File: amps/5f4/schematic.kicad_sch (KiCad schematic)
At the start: 66 parts, among them T3 45216

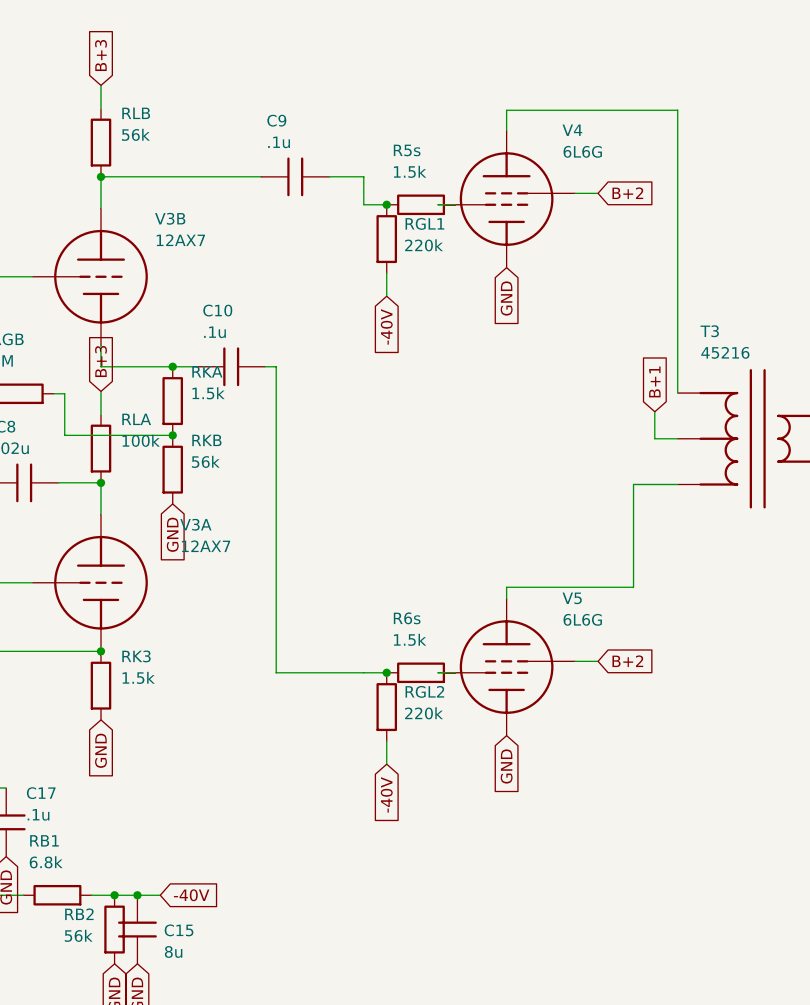
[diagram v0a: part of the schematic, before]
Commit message: Fix: schematic wiring on 5c1, 5e1, 5e4a, 5e5a, 5e6a, 5f4; all six claim equivalence
- 5c1, 5e1: the B+1/B+2/B+3 labels sat 3.56 mm above the filter chain with
  no lead, naming rails the drawing never reached
- 5e4a, 5e5a, 5e6a, 5f4: the 220k grid leak tapped the coupling-cap node;
  the netlist and the factory-derived layouts both return it at the grid
  pin after the 1.5k stopper (coupler -> stopper -> grid, as jtm45 draws
  it); each stopper now lands on the pentode's own grid pin and the leak
  hangs off that junction
- sch_map.yaml schematic_claim: verified on all six -> 37 of 38 sheets are
  hard-gated; 6g5 stays unclaimed (presence-branch DC path is a source
  question, not a declaration)

Co-Authored-By: Claude Fable 5.1 <noreply@anthropic.com>
Claude-Session: https://claude.ai/code/session_01KBMfdh37HmCL2iWcBiL5J1
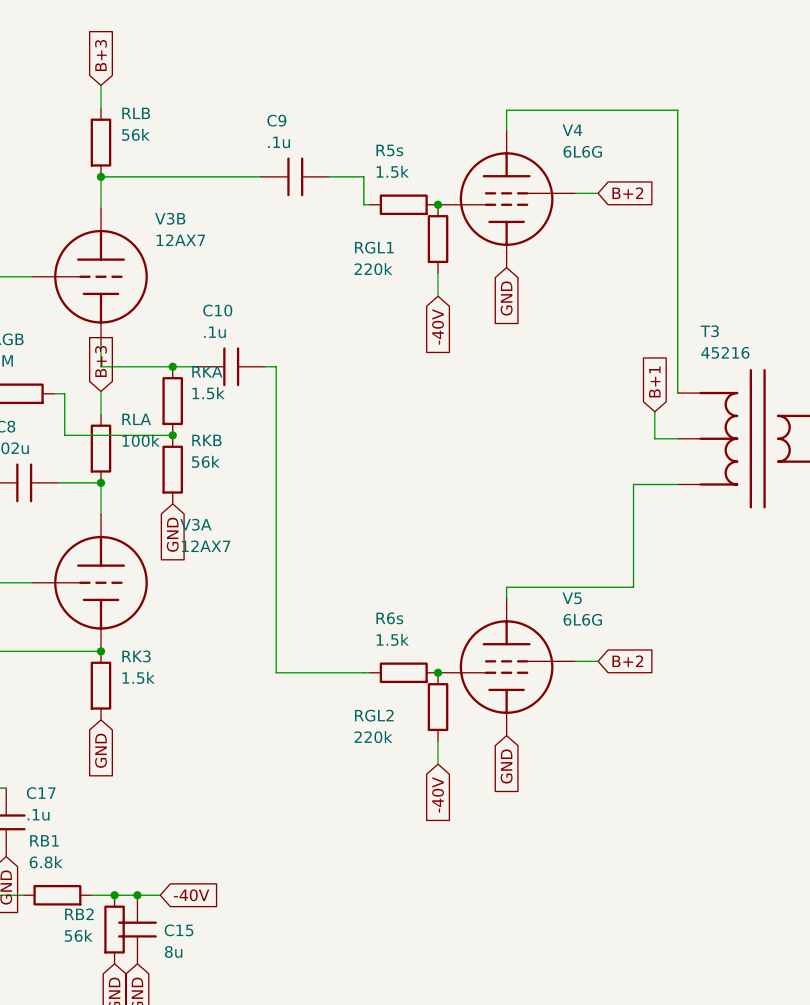
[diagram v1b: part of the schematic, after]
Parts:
- removed RB1: 6.8k, symbol cx:R
- removed RD1, RD2: 10k, symbol cx:R
- added C12, C13: 16u, symbol cx:C
- added D1: SEL, symbol cx:DIODE_SS
- RB1: renamed from D1; value SEL -> 6.8k; symbol cx:DIODE_SS -> cx:R
- RD1: renamed from C12; value 16u -> 10k; symbol cx:C -> cx:R
- RD2: renamed from C13; value 16u -> 10k; symbol cx:C -> cx:R
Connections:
- net -40V: now also RB1.2
- net B+2: now also C12.1
- net B+3: now also RD1.2, C13.1
- net B+4: now also RD2.2
- net GND: now also C12.2, C13.2; no longer RD1.2, RD2.2
- net HT_B: now also D1.1 (A); no longer RB1.1 (A)
- net at C9.2, R5s.1: no longer RGL1.1
- net at R6s.2, V5.2 (G1): now also RGL2.1
- net at R5s.2, V4.2 (G1): now also RGL1.1
- net at C10.2, R6s.1: no longer RGL2.1
- new net: D1.2 (K), RB1.1
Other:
- moved on the sheet: R5s
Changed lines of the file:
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@@
   (wire (pts (xy 196.758 27.178) (xy 196.758 30.278))
     (stroke (width 0) (type default)))
-  (wire (pts (xy 196.758 30.278) (xy 199.298 30.278))
-    (stroke (width 0) (type default)))
-  (symbol (lib_id "cx:R") (at 203.108 30.278 90) (unit 1)
-    (in_bom yes) (on_board yes)
-    (property "Reference" "R5s" (at 199.908 24.278 270) (effects (font (size 1.27 1.27)) (justify left)))
-    (property "Value" "1.5k" (at 199.908 26.678 270) (effects (font (size 1.27 1.27)) (justify left))))
   (symbol (lib_id "cx:PENTODE") (at 212.618 29.643 0) (unit 1)
     (in_bom yes) (on_board yes)
     (property "Reference" "V4" (at 218.818 22.043 0) (effects (font (size 1.27 1.27)) (justify left)))
     (property "Value" "6L6G" (at 218.818 24.443 0) (effects (font (size 1.27 1.27)) (justify left))))
-  (wire (pts (xy 206.918 30.278) (xy 204.998 30.278))
+  (symbol (lib_id "cx:R") (at 201.188 30.278 90) (unit 1)
+    (in_bom yes) (on_board yes)
+    (property "Reference" "R5s" (at 197.988 24.278 270) (effects (font (size 1.27 1.27)) (justify left)))
+    (property "Value" "1.5k" (at 197.988 26.678 270) (effects (font (size 1.27 1.27)) (justify left))))
+  (wire (pts (xy 196.758 30.278) (xy 197.378 30.278))
     (stroke (width 0) (type default)))
-  (junction (at 199.298 30.278) (diameter 0) (color 0 0 0 0))
-  (symbol (lib_id "cx:R") (at 199.298 34.088 0) (unit 1)
+  (junction (at 204.998 30.278) (diameter 0) (color 0 0 0 0))
+  (symbol (lib_id "cx:R") (at 204.998 34.088 0) (unit 1)
     (in_bom yes) (on_board yes)
-    (property "Reference" "RGL1" (at 201.214 32.448 0) (effects (font (size 1.27 1.27)) (justify left)))
-    (property "Value" "220k" (at 201.214 34.848 0) (effects (font (size 1.27 1.27)) (justify left))))
-  (wire (pts (xy 199.298 37.898) (xy 199.298 40.438))
+    (property "Reference" "RGL1" (at 195.598 35.088 0) (effects (font (size 1.27 1.27)) (justify left)))
+    (property "Value" "220k" (at 195.598 37.488 0) (effects (font (size 1.27 1.27)) (justify left))))
+  (wire (pts (xy 204.998 37.898) (xy 204.998 40.438))
     (stroke (width 0) (type default)))
-  (global_label "-40V" (shape input) (at 199.298 40.438 270)
+  (global_label "-40V" (shape input) (at 204.998 40.438 270)
     (effects (font (size 1.27 1.27)) (justify right)))
   (wire (pts (xy 220.238 29.008) (xy 222.778 29.008))
@@
   (wire (pts (xy 187.018 82.278) (xy 196.758 82.278))
     (stroke (width 0) (type default)))
-  (wire (pts (xy 196.758 82.278) (xy 199.298 82.278))
-    (stroke (width 0) (type default)))
-  (symbol (lib_id "cx:R") (at 203.108 82.278 90) (unit 1)
-    (in_bom yes) (on_board yes)
-    (property "Reference" "R6s" (at 199.908 76.278 270) (effects (font (size 1.27 1.27)) (justify left)))
-    (property "Value" "1.5k" (at 199.908 78.678 270) (effects (font (size 1.27 1.27)) (justify left))))
   (symbol (lib_id "cx:PENTODE") (at 212.618 81.643 0) (unit 1)
     (in_bom yes) (on_board yes)
     (property "Reference" "V5" (at 218.818 74.043 0) (effects (font (size 1.27 1.27)) (justify left)))
     (property "Value" "6L6G" (at 218.818 76.443 0) (effects (font (size 1.27 1.27)) (justify left))))
-  (wire (pts (xy 206.918 82.278) (xy 204.998 82.278))
+  (symbol (lib_id "cx:R") (at 201.188 82.278 90) (unit 1)
+    (in_bom yes) (on_board yes)
+    (property "Reference" "R6s" (at 197.988 76.278 270) (effects (font (size 1.27 1.27)) (justify left)))
+    (property "Value" "1.5k" (at 197.988 78.678 270) (effects (font (size 1.27 1.27)) (justify left))))
+  (wire (pts (xy 196.758 82.278) (xy 197.378 82.278))
     (stroke (width 0) (type default)))
-  (junction (at 199.298 82.278) (diameter 0) (color 0 0 0 0))
-  (symbol (lib_id "cx:R") (at 199.298 86.088 0) (unit 1)
+  (junction (at 204.998 82.278) (diameter 0) (color 0 0 0 0))
+  (symbol (lib_id "cx:R") (at 204.998 86.088 0) (unit 1)
     (in_bom yes) (on_board yes)
-    (property "Reference" "RGL2" (at 201.214 84.448 0) (effects (font (size 1.27 1.27)) (justify left)))
-    (property "Value" "220k" (at 201.214 86.848 0) (effects (font (size 1.27 1.27)) (justify left))))
-  (wire (pts (xy 199.298 89.898) (xy 199.298 92.438))
+    (property "Reference" "RGL2" (at 195.598 87.088 0) (effects (font (size 1.27 1.27)) (justify left)))
+    (property "Value" "220k" (at 195.598 89.488 0) (effects (font (size 1.27 1.27)) (justify left))))
+  (wire (pts (xy 204.998 89.898) (xy 204.998 92.438))
     (stroke (width 0) (type default)))
-  (global_label "-40V" (shape input) (at 199.298 92.438 270)
+  (global_label "-40V" (shape input) (at 204.998 92.438 270)
     (effects (font (size 1.27 1.27)) (justify right)))
   (wire (pts (xy 220.238 81.008) (xy 222.778 81.008))

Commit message: Add: real tube pin numbers and readable valve glyphs on every schematic
Phase B of the drawing program. A factory service sheet numbers every tube
pin, because the number is what a technician puts a probe on. This corpus
printed none, and the numbers hidden in its symbols were positional
placeholders (P=1, G=2, K=3) that would have published a 6V6GT's plate as
pin 1 when it is pin 3.

1055 electrodes now carry the real number, 1027 lettered (27 are shared
filaments deduped, 1 dropped for want of clear space on the 6G2). Resolved per
instance from reference/tubes/<slug>.yaml through the same alias resolution the
layout renderer uses, so a 12AX7 section and a 6SL7 section each get their own
basing. A valve whose basing the corpus does not carry prints nothing rather
than a wrong number.

Section letters and basing units are now separate things, which cost a detour
worth recording. The RCA 12AX7-A sheet reads "Pin 1 - Plate of Unit No.2 ...
Pin 6 - Plate of Unit No.1", so unit numbering is not pin order; the 5Y3 and
GZ34 number their units in opposite pin order, so nothing positional can
express it. But the section LETTER is a designator, not a basing fact: this
corpus, like every technician, calls the first stage in signal order V1A, and
five amps' prose already did. On four amps the factory sheets put that first
stage on the other half -- the AA764's own schematic prints +200 V on pin 1 --
so those drawings now state their unit explicitly, each citing its source, and
no letter, netlist, parts list or layout comment changed. 183 layout comments
agree with the printed numbers, 0 disagree. A guard fires if two halves of one
bottle resolve to the same unit, which is exactly how this was found.

Glyphs: the cathode gains a bracket and filament hairpin so it can no longer be
confused with the plate bar, the pentode's screen sits on its own row, and a
rectifier draws as one envelope over its sections instead of two apparent
bottles. Line weights are scaled per sheet to a co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
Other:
- note added: "1"
- note added: "2"
- note added: "2,8"
- note added: "3"
- note added: "4"
- note added: "5"
- note added: "6"
- note added: "7"
- note added: "8"

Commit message: Fix: schematic sheet notes no longer name repository files
Thirty-seven committed sheets rendered footnotes and section notes such as
"Heaters and PT primary omitted — see netlist.cir and meta.yaml" or
"excluded from netlist.cir (notes.md)" to visitors through KiCanvas. The
prose sweeps never counted sheets. Rewritten in the site's own words — the
netlist, the sources list, the circuit story, the parts list, the board
drawing — in 59 strings across 33 draw scripts, keeping every technical
claim as it was; the three tone sheets (6G4, 6G5, 6G6-B) are under repair
elsewhere and keep theirs for now. The sweep touched only strings passed to
the sheet's note, text, caption and footnote calls, never a path or a value.

Gates: check_schematics 40/0, connectivity 0 isolated pins;
verify_schematic_nets 40 clean; only the regenerated sheets and their served
copies changed.

Co-Authored-By: Claude Fable 5.1 <noreply@anthropic.com>
Claude-Session: https://claude.ai/code/session_01KBMfdh37HmCL2iWcBiL5J1
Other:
- note added: "Heaters, PT primary and standby omitted — see the netlist and the sources list"
- note removed: "Heaters, PT primary and standby omitted — see netlist.cir and meta.yaml"
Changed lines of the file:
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@@
   (text "4" (at 46.478 107.708 0)
     (effects (font (size 1.1 1.1)) (justify left)))
-  (text "Heaters, PT primary and standby omitted — see netlist.cir and meta.yaml" (at 12.7 142.856 0)
+  (text "Heaters, PT primary and standby omitted — see the netlist and the sources list" (at 12.7 142.856 0)
     (effects (font (size 1.2 1.2)) (justify left)))
   (sheet_instances (path "/" (page "1")))

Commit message: Fix: state the datasheet unit on 17 dual-triode sections whose sheets printed the other half's pin numbers
The sheet-vs-board gate reported these sockets as SECTION-SWAP; the
2026-09-10 source-read triage found the BOARD right on every one of them
(and both surfaces wrong on the 5G9 tremolo bottle). Each sheet had
lettered the section on the default map (A -> unit 1 -> pins 6/7/8) where
the factory drawing puts that stage on 1/2/3. The draw scripts now state
`unit=` on both halves, with the source cited beside the call, so the
printed socket numbers are the factory's:

- 5f4 V3: driver V3A -> 1/2/3, cathodyne V3B -> 6/7/8
  (crop 5f4-V3-layout-trace.png: +213 V driver plate -> pin 1, +270 V -> 6)
- 5f8a V3: 82k half V3A -> 1/2/3, 100k half V3B -> 6/7/8
  (crop 5f8a-V3-layout-trace.png: +225 -> 6, +19 -> 2, +28.5 -> 8)
- 6161 V1: channel 1 V1A -> 1/2/3 (crop 6161-V1-ch1.png prints 1/2/3);
  6161 V2: 1 MEG-grid half V2A -> 1/2/3, paraphase V2B -> 6/7/8
  (crop 6161-V2.png / 6161-V2-right.png)
- 6g3 V3: 82k half V3A -> 1/2/3 (crop 6g3-V3-layout-wires.png: +230 -> 1,
  +225 -> 6, +20 -> 7)
- aa1164 V3: recovery V3A -> 1/2/3, mixer V3B -> 6/7/8
  (crops aa1164-V3A-recovery-schem.png, aa1164-V3B-mixer-schem.png)
- aa864-bassman V1/V2: input stages 2/1/3, second stages 7/6/8; V4: the
  .1/500 pF-fed 82k half 2/1/3 (crops aa864-V1A-input.png,
  aa864-V1B-second.png, aa864-V2A-input.png, aa864-V2B-second.png,
  aa864-V4-PI.png)
- ab165 V1/V2/V4: same pattern (crops ab165-V1A-input.png,
  ab165-V1B-second.png, ab165-V2A-input.png, ab165-V2B-second.png,
  ab165-V4-PI.png)
- ab763-super V1/V2: slope-plate +270 V -> pin 1 (input stage), .047
  plate -> 6 (crops ab763-super-V1-layout-sh.png, ab763-super-V2-layout-sh.png)
- dr103 V2/V3: gain stages 6/7/8, cathode followers 1/2/3 (crops
  dr103-V2-huss.png, dr103-V3-huss.png — the Huss redraw, not a factory
  print; noted in the script)
- 5g9 V3: oscillator V3A -> 1/2/3, follower V3B -> 6/7/8 (crops
  5g9-V3-strap71-zoom.png, 5g9-V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
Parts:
- V3A: Basing_unit (none) -> 2
- V3B: Basing_unit (none) -> 1
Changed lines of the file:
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@@
     (in_bom yes) (on_board yes)
     (property "Reference" "V3A" (at 176.348 65.878 0) (effects (font (size 1.27 1.27)) (justify left)))
-    (property "Value" "12AX7" (at 176.348 68.278 0) (effects (font (size 1.27 1.27)) (justify left))))
+    (property "Value" "12AX7" (at 176.348 68.278 0) (effects (font (size 1.27 1.27)) (justify left)))
+    (property "Basing_unit" "2" (at 176.348 70.678 0) (effects (font (size 1.27 1.27)) hide)))
   (wire (pts (xy 154.018 72.278) (xy 159.928 72.278))
     (stroke (width 0) (type default)))
@@
     (in_bom yes) (on_board yes)
     (property "Reference" "V3B" (at 173.548 31.878 0) (effects (font (size 1.27 1.27)) (justify left)))
-    (property "Value" "12AX7" (at 173.548 34.278 0) (effects (font (size 1.27 1.27)) (justify left))))
+    (property "Value" "12AX7" (at 173.548 34.278 0) (effects (font (size 1.27 1.27)) (justify left)))
+    (property "Basing_unit" "1" (at 173.548 36.678 0) (effects (font (size 1.27 1.27)) hide)))
   (wire (pts (xy 167.548 64.658) (xy 167.548 61.178))
     (stroke (width 0) (type default)))
@@
   (text "3" (at 108.708 61.628 0)
     (effects (font (size 1.1 1.1)) (justify left)))
-  (text "6" (at 168.398 65.928 0)
-    (effects (font (size 1.1 1.1)) (justify left)))
-  (text "7" (at 160.601 70.878 0)
-    (effects (font (size 1.1 1.1)) (justify left)))
-  (text "8" (at 168.398 78.628 0)
-    (effects (font (size 1.1 1.1)) (justify left)))
-  (text "1" (at 168.398 31.928 0)
-    (effects (font (size 1.1 1.1)) (justify left)))
-  (text "2" (at 160.601 36.878 0)
-    (effects (font (size 1.1 1.1)) (justify left)))
-  (text "3" (at 169.848 44.628 0)
+  (text "1" (at 168.398 65.928 0)
+    (effects (font (size 1.1 1.1)) (justify left)))
+  (text "2" (at 160.601 70.878 0)
+    (effects (font (size 1.1 1.1)) (justify left)))
+  (text "3" (at 168.398 78.628 0)
+    (effects (font (size 1.1 1.1)) (justify left)))
+  (text "6" (at 168.398 31.928 0)
+    (effects (font (size 1.1 1.1)) (justify left)))
+  (text "7" (at 160.601 36.878 0)
+    (effects (font (size 1.1 1.1)) (justify left)))
+  (text "8" (at 169.848 44.628 0)
     (effects (font (size 1.1 1.1)) (justify left)))
   (text "3" (at 213.468 23.293 0)

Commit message: Fix: draw the 1 MΩ input grid leak on the jack-1 tip node, not the grid, on eight tweed/Champ sheets
Every tweed and Champ factory sheet hangs the 1 MΩ from the jack-1 tip
node (the node the jack-2 shorting contact also lands on) to ground, and
runs the 68 K stoppers from the jack tips to the grid. These eight sheets
drew the 1 MΩ on the GRID side of the stopper — one copy-pasted idiom in
four scripts and its cousins in four more; there is no shared helper, so
each script is fixed where it draws the block. The stopper is declared
DC-transparent (layout net_map.series_bridge), so the netlist sees one node
either way and verify_schematic_nets stays 40 clean; the sheet-vs-board
gate, which compares the drawings to each other, drops all twelve
MISPLACED findings (RG1/RG2 on 5e4a, 5e5a, 5f4, 5f6; R3 on 5f2a, aa764,
aa764-vibro; R1 on 5f1). 5f10's jack chain is a separate task.

Crops read: 5e4a-RG1-RG2-input.png, 5e5a-RG1-RG2-input.png,
5f4-RG1-input.png, 5f6-RG1-RG2-input.png, 5f2a-R3-input.png,
5f1-R1-input.png, aa764-R3-input.png, aa764-vibro-R3-input.png — each
prints "1 MEG." from the jack-1 tip to ground with the 68K pair to the grid.

Geometry: the four two-channel sheets hang the leak from the stopper's
jack-side pin; 5f1 drops it from the INPUT line; 5f2a and the two Champs
stand it upward off the jack-1 line because the jack-2 line runs 8–12 mm
below. Previews read cleanly. The circuit stories already say the leaks
mount at the jacks, so no prose changed.

Gates: check_schematics 40/0 (0 isolated), verify_schematic_nets 40
clean, validate/value-consistency/era-values clean, regenerate-all leaves
every other sheet byte-identical. verify_sheet_vs_board misplaced 98 -> 86.

Co-Authored-By: Claude Fable 5.1 <noreply@anthropic.com>
Claude-Session: https://claude.ai/code/session_01KBMfdh37HmCL2iWcBiL5J1
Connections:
- net CH1: now also RG1.1
- net CH2: now also RG2.1
- net at R1s.2, V1A.2 (G): no longer RG1.1
- net at R2s.2, V1B.2 (G): no longer RG2.1
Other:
- moved on the sheet: RG1, RG2
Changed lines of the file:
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@@
   (wire (pts (xy 29.118 38.278) (xy 32.928 38.278))
     (stroke (width 0) (type default)))
-  (junction (at 29.118 38.278) (diameter 1.013) (color 0 0 0 0))
-  (symbol (lib_id "cx:R") (at 29.118 42.088 0) (unit 1)
+  (junction (at 21.498 38.278) (diameter 1.013) (color 0 0 0 0))
+  (symbol (lib_id "cx:R") (at 21.498 42.088 0) (unit 1)
     (in_bom yes) (on_board yes)
-    (property "Reference" "RG1" (at 31.318 38.888 0) (effects (font (size 1.27 1.27)) (justify left)))
-    (property "Value" "1M" (at 31.318 41.288 0) (effects (font (size 1.27 1.27)) (justify left))))
-  (global_label "GND" (shape input) (at 29.118 45.898 270)
+    (property "Reference" "RG1" (at 23.698 42.088 0) (effects (font (size 1.27 1.27)) (justify left)))
+    (property "Value" "1M" (at 23.698 44.488 0) (effects (font (size 1.27 1.27)) (justify left))))
+  (global_label "GND" (shape input) (at 21.498 45.898 270)
     (effects (font (size 1.27 1.27)) (justify right)))
   (wire (pts (xy 40.548 30.658) (xy 40.548 27.178))
@@
   (wire (pts (xy 29.118 72.278) (xy 32.928 72.278))
     (stroke (width 0) (type default)))
-  (junction (at 29.118 72.278) (diameter 1.013) (color 0 0 0 0))
-  (symbol (lib_id "cx:R") (at 29.118 76.088 0) (unit 1)
+  (junction (at 21.498 72.278) (diameter 1.013) (color 0 0 0 0))
+  (symbol (lib_id "cx:R") (at 21.498 76.088 0) (unit 1)
     (in_bom yes) (on_board yes)
-    (property "Reference" "RG2" (at 31.318 72.888 0) (effects (font (size 1.27 1.27)) (justify left)))
-    (property "Value" "1M" (at 31.318 75.288 0) (effects (font (size 1.27 1.27)) (justify left))))
-  (global_label "GND" (shape input) (at 29.118 79.898 270)
+    (property "Reference" "RG2" (at 23.698 76.088 0) (effects (font (size 1.27 1.27)) (justify left)))
+    (property "Value" "1M" (at 23.698 78.488 0) (effects (font (size 1.27 1.27)) (justify left))))
+  (global_label "GND" (shape input) (at 21.498 79.898 270)
     (effects (font (size 1.27 1.27)) (justify right)))
   (wire (pts (xy 40.548 64.658) (xy 40.548 61.178))
